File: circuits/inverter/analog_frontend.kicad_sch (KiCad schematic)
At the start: 104 parts

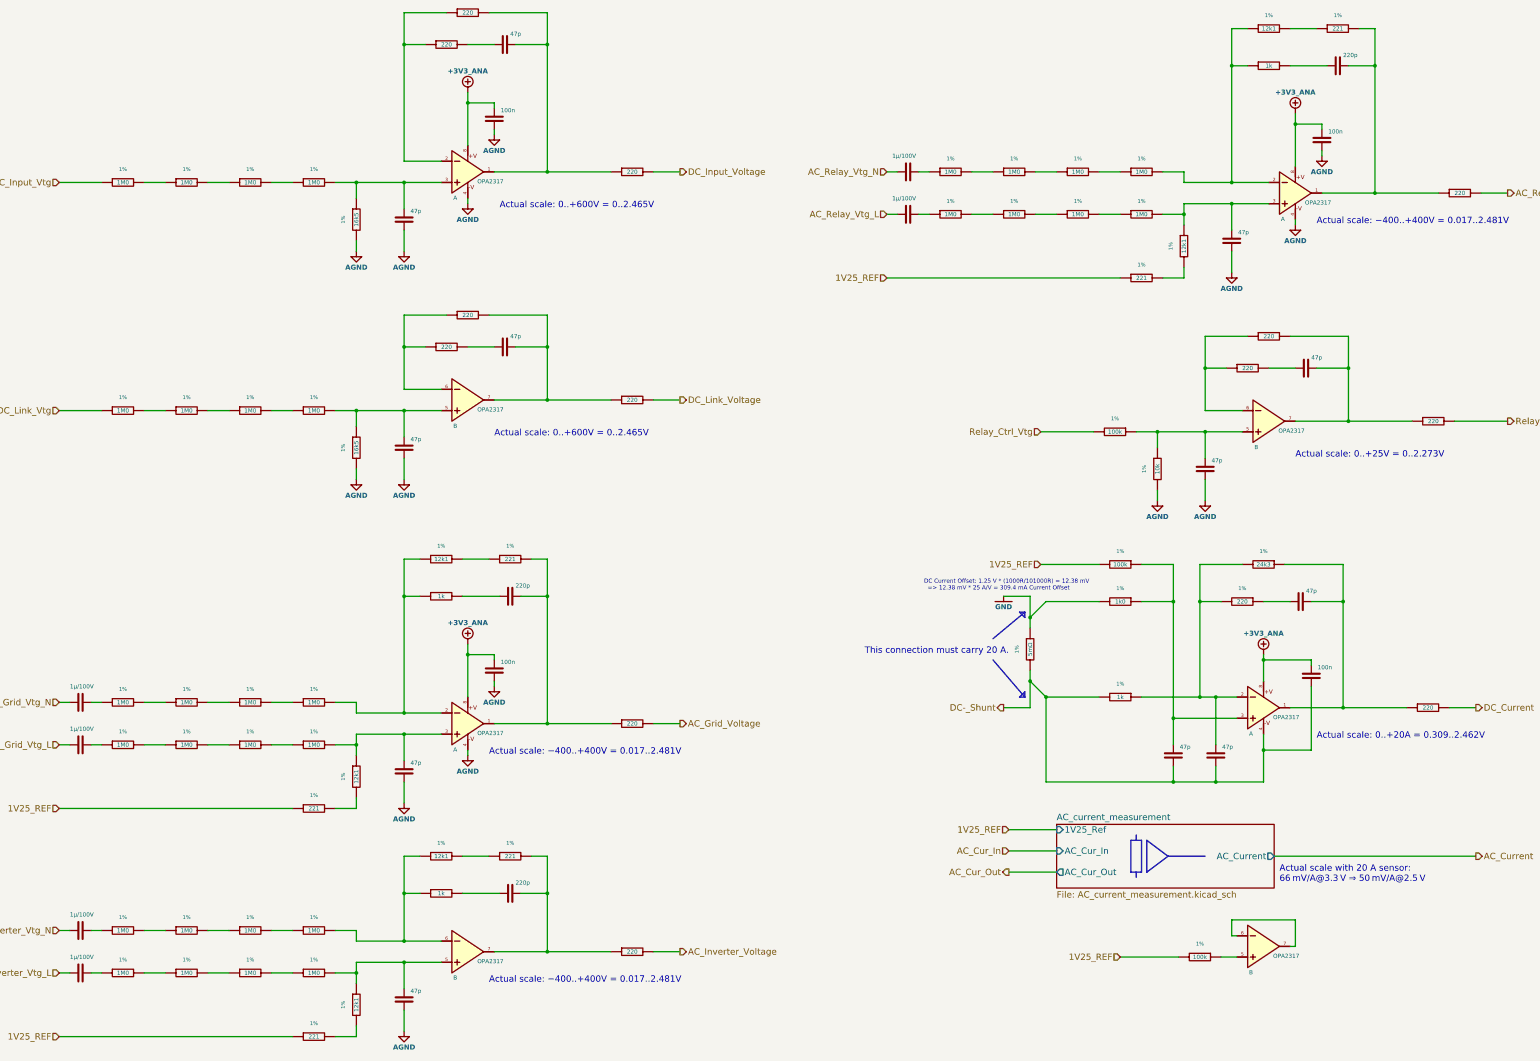
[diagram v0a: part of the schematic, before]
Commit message: converts libraries to Kicad 6 format, updates bridge driver
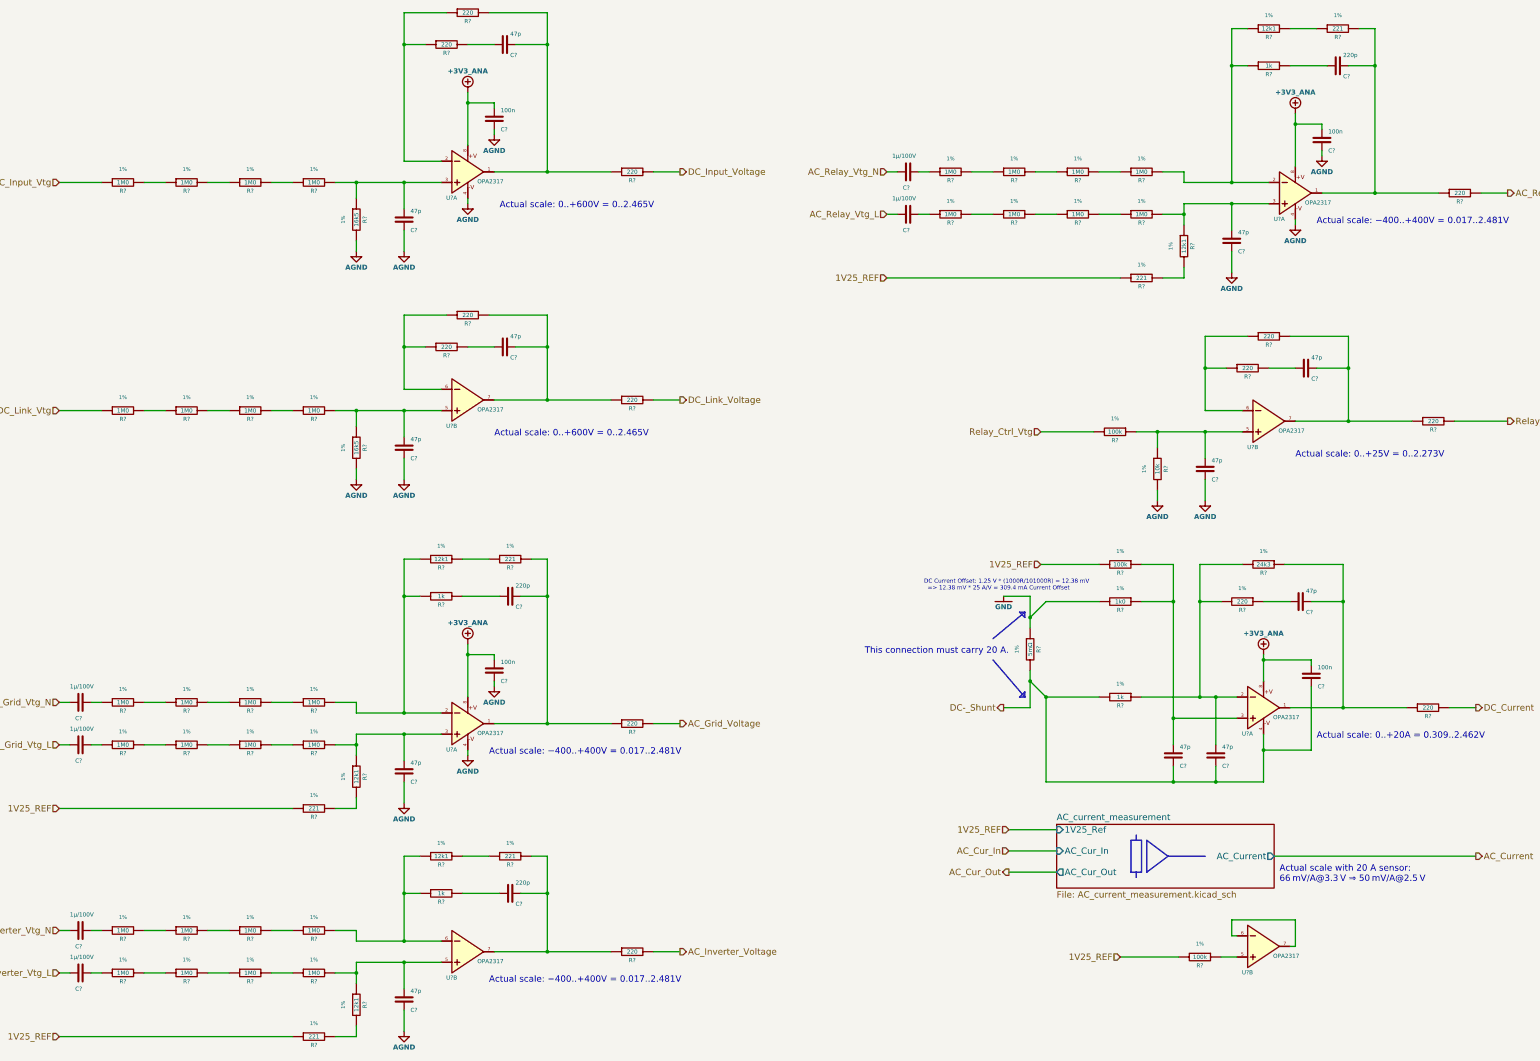
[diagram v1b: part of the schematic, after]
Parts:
- gave numbers to parts that had none: 3
